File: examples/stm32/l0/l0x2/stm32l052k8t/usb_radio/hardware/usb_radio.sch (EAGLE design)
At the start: 48 parts, among them IC1 SI4737-C40-GU, IC2 LM4861M, IC3 LM4861M, M1 STM32L052K8T_DIP, Q1 32.768kHz, U1 MC1213A-01SO, X1 MINI-USB-UX60A-MB-5ST, X2 B6251F1-NT3G-50, X3 MKDSN1,5/2-5,08, X4 MKDSN1,5/2-5,08

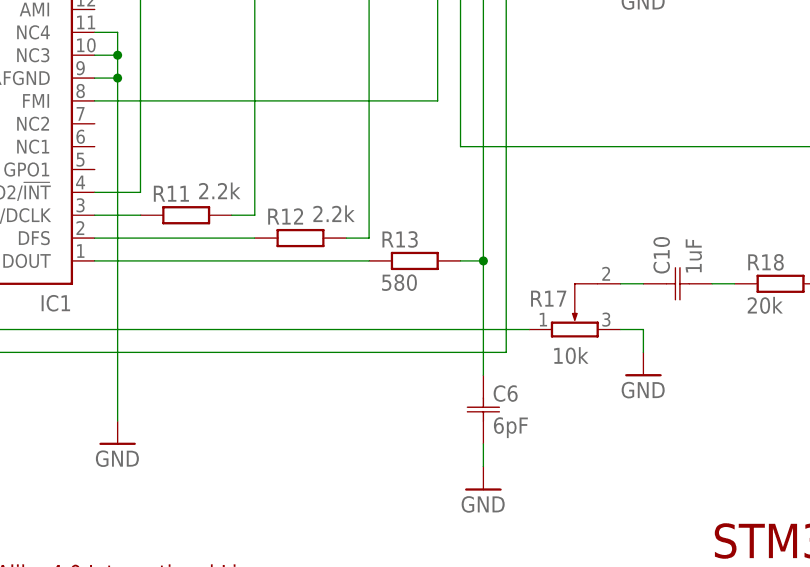
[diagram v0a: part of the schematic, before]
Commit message: Fix usb_radio hardware.
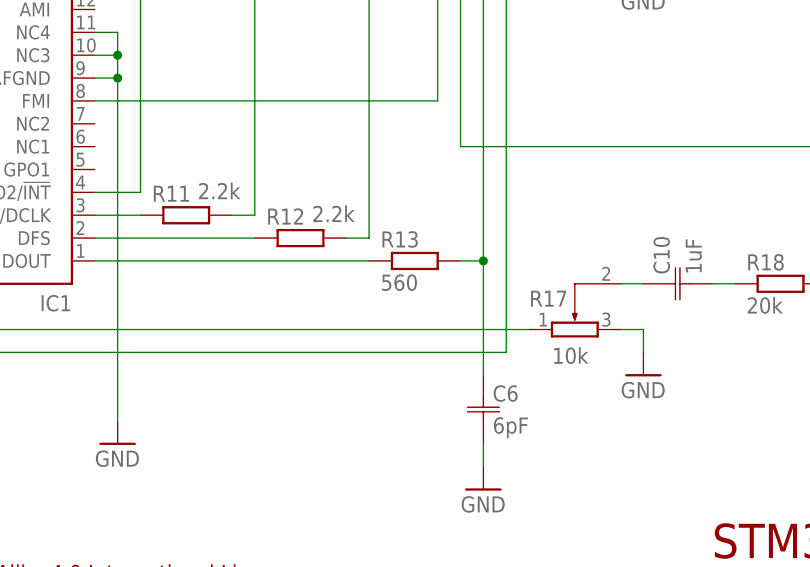
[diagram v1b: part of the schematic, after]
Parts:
- R13: value 580 -> 560
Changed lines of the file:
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@@
 <?xml version="1.0" encoding="utf-8"?>
 <!DOCTYPE eagle SYSTEM "eagle.dtd">
-<eagle version="7.6.0">
+<eagle version="7.7.0">
 <drawing>
 <settings>
@@
 <part name="R11" library="resistor" deviceset="R-EU_" device="0207/2V" value="2.2k"/>
 <part name="R12" library="resistor" deviceset="R-EU_" device="0207/2V" value="2.2k"/>
-<part name="R13" library="resistor" deviceset="R-EU_" device="0207/2V" value="580"/>
+<part name="R13" library="resistor" deviceset="R-EU_" device="0207/2V" value="560"/>
 <part name="C6" library="cap" deviceset="C-JIS" device="050-024X044" value="6pF"/>
 <part name="JP2" library="jumper" deviceset="JP1E" device=""/>
